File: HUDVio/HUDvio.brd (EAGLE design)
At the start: 85 x 54 mm, 16 parts, among them U1 ST_STM32F446RET7, U3 TVP5150AM1PBSR, X1 ABRACON_ABM8-27.000MHZ

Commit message: Lots of shit. Added splitter
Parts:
- added C10: 30PF_0805, Skyhawkson-Capacitors:KEMET_0805
- added C11, C12, C13: 1UF_0805, Skyhawkson-Capacitors:KEMET_0805
- added C14, C15, C16, C17, C18, C19, C20, C4, C7, C8, C9: 100NF_0805, Skyhawkson-Capacitors:KEMET_0805
- added C5, C6: 10UF_0805, Skyhawkson-Capacitors:KEMET_0805
- added R10, R11, R12, R16, R18, R9: 1K_0603, Skyhawkson-Resistors:0603
- added R13: 0R_0603, Skyhawkson-Resistors:0603
- added R14, R15: 37R4_0603, Skyhawkson-Resistors:0603
- added R17, R7, R8: 75R_0603, Skyhawkson-Resistors:0603
- added U4: NEXPERIA_NVT2006, Skyhawkson-ICs:NEXPERIA_SOT403-1_(TSSOP16)
- added U5: MAXIM_MAX4389, Skyhawkson-RF:MAXIM_21-0058_(SOT23-6)
- added X2: ABRACON_ABM8-14.31818MHZ, Skyhawkson-Miscellaneous:ABRACON_ABM8
- C1: value 1UF_0805 -> 30PF_0805
- moved C1 67.7 mm to (-76.0, -79.0)
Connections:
- removed net AGND: U2.20, U3.3, U3.31, U3.7
- removed net AVDD: U2.21, U3.32, U3.4
- removed net DGND: U3.19
- removed net DVDD: U3.20
- removed net IO_DVDD: U3.10
- removed net PGND: U2.23
- removed net PVDD: U2.24
- removed net VIDEO-OUT: U$3.3
- new net $NET11: C7.P$2, R13.1, R7.1
- new net +1V8: C16.P$2, C17.P$2, C18.P$2, C19.P$2, U3.20, U3.32, U3.4
- new net +3V3: C14.P$2, R11.1, U3.10, U4.2
- new net 5150-IN: C20.P$2, U3.1
- new net ACTIVE-VID: U3.26
- new net CS-LV: U4.3
- new net FID/GLCO: U3.23
- new net LOS-LV: U4.7
- new net LOSS-OF-SYNC: R9.1, U2.12, U4.10
- new net MAX7456-OUT: R8.2
- new net MISO-LV: U4.6
- new net MOSI-LV: U4.4
- new net N$10: C5.P$2, C6.P$2, R8.1
- new net N$11: C20.P$1, R14.2, R15.2
- new net N$12: C15.P$2, U3.2
- new net N$13: R16.1, U4.16
- new net N$14: U5.3
- new net N$15: R18.1, U5.4
- new net N$6: R10.2, U3.8
- new net N$7: R12.2, U3.28
- new net N$8: C11.P$1, C13.P$1, U3.30
- new net N$9: C11.P$2, C12.P$2, U3.29
- new net SAG: C6.P$1, U2.25
- new net SCLK-LV: U4.5
- new net SPLITTER-OUT: R14.1, R17.1, U5.1
- new net SYSCLK: U3.9
- new net VBLANK: U3.27
- new net VIDIN: C7.P$1, U2.22
- new net VIDOUT: C5.P$1, U2.26
- new net VTX-OUT: R17.2, U$3.3
- new net XTAL1: C1.P$1, U3.5, X2.1
- new net XTAL2: C10.P$1, U3.6, X2.3
- new net YOUT0: U3.18
- new net YOUT1: U3.17
- new net YOUT2: U3.16
- new net YOUT3: U3.15
- new net YOUT4: U3.14
- new net YOUT5: U3.13
- new net YOUT6: U3.12
- new net YOUT7: R11.2, U3.11
- net +5V: now also C4.P$2, C8.P$2, C9.P$2, R10.1, R12.1, R16.2, R9.2, U2.21, U2.24, U4.15, U5.6; no longer C1.P$2
- net GND: now also C1.P$2, C10.P$2, C12.P$1, C13.P$2, C14.P$1, C15.P$1, C16.P$1, C17.P$1, C18.P$1, C19.P$1, C4.P$1, C8.P$1, C9.P$1, R15.1, R18.2, R7.2, U2.20, U2.23, U3.19, U3.3, U3.31, U3.7, U4.1, U5.2, X2.2, X2.4; no longer C1.P$1
- net MAX7456-CS: now also U4.14
- net MISO: now also U4.11
- net MOSI: now also U4.13
- net SCLK: now also U4.12
- net VIDEO-IN: now also R13.2

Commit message: Ran DCMI pins
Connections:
- new net DCMI_HSYNC: U1.20, U3.25
- new net DCMI_VSYNC: U1.59, U3.24
- net SYSCLK: now also U1.22
- net YOUT0: now also U1.37
- net YOUT1: now also U1.38
- net YOUT2: now also U1.39
- net YOUT3: now also U1.40
- net YOUT4: now also U1.52
- net YOUT5: now also U1.58
- net YOUT6: now also U1.61
- net YOUT7: now also U1.62
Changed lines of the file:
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@@
 <contactref element="R5" pad="2"/>
 </signal>
-<signal name="VIDIN">
+<signal name="VIDIN" class="1">
 <contactref element="U2" pad="22"/>
 <contactref element="C7" pad="P$1"/>
 <wire x1="-61.1265" y1="-13.675" x2="-71.925" y2="-61" width="0" layer="19" extent="1-1"/>
 </signal>
-<signal name="VIDOUT">
+<signal name="VIDOUT" class="1">
 <contactref element="U2" pad="26"/>
 <contactref element="C5" pad="P$1"/>
 <wire x1="-61.1265" y1="-11.075" x2="-71.925" y2="-55" width="0" layer="19" extent="1-1"/>
 </signal>
-<signal name="MAX7456-OUT">
+<signal name="MAX7456-OUT" class="1">
 <contactref element="R8" pad="2"/>
 </signal>
@@
 <signal name="SYSCLK">
 <contactref element="U3" pad="9"/>
+<contactref element="U1" pad="22"/>
+<wire x1="-26.65" y1="3.14" x2="-47.75" y2="3.8046" width="0" layer="19" extent="1-1"/>
 </signal>
 <signal name="XTAL1">
@@
 <contactref element="R11" pad="2"/>
 <contactref element="U3" pad="11"/>
+<contactref element="U1" pad="62"/>
 <wire x1="-46.75" y1="3.8046" x2="-75.15" y2="-85" width="0" layer="19" extent="1-1"/>
+<wire x1="-28.15" y1="14.64" x2="-46.75" y2="3.8046" width="0" layer="19" extent="1-1"/>
 </signal>
 <signal name="YOUT0">
 <contactref element="U3" pad="18"/>
+<contactref element="U1" pad="37"/>
+<wire x1="-19.65" y1="7.14" x2="-42.8046" y2="5.75" width="0" layer="19" extent="1-1"/>
 </signal>
 <signal name="YOUT1">
 <contactref element="U3" pad="17"/>
+<contactref element="U1" pad="38"/>
+<wire x1="-19.65" y1="7.64" x2="-42.8046" y2="5.25" width="0" layer="19" extent="1-1"/>
 </signal>
 <signal name="YOUT2">
 <contactref element="U3" pad="16"/>
+<contactref element="U1" pad="39"/>
+<wire x1="-19.65" y1="8.14" x2="-44.25" y2="3.8046" width="0" layer="19" extent="1-1"/>
 </signal>
 <signal name="YOUT3">
 <contactref element="U3" pad="15"/>
+<contactref element="U1" pad="40"/>
+<wire x1="-19.65" y1="8.64" x2="-44.75" y2="3.8046" width="0" layer="19" extent="1-1"/>
 </signal>
 <signal name="YOUT4">
 <contactref element="U3" pad="14"/>
+<contactref element="U1" pad="52"/>
+<wire x1="-23.15" y1="14.64" x2="-45.25" y2="3.8046" width="0" layer="19" extent="1-1"/>
 </signal>
 <signal name="YOUT5">
 <contactref element="U3" pad="13"/>
+<contactref element="U1" pad="58"/>
+<wire x1="-26.15" y1="14.64" x2="-45.75" y2="3.8046" width="0" layer="19" extent="1-1"/>
 </signal>
 <signal name="YOUT6">
 <contactref element="U3" pad="12"/>
+<contactref element="U1" pad="61"/>
+<wire x1="-27.65" y1="14.64" x2="-46.25" y2="3.8046" width="0" layer="19" extent="1-1"/>
 </signal>
 <signal name="FID/GLCO">
@@
 <wire x1="-46.25" y1="10.1954" x2="-75.075" y2="-91" width="0" layer="19" extent="1-1"/>
 </signal>
-<signal name="5150-IN">
+<signal name="5150-IN" class="1">
 <contactref element="U3" pad="1"/>
 <contactref element="C20" pad="P$2"/>
@@
 <contactref element="U5" pad="3"/>
 </signal>
-<signal name="SPLITTER-OUT">
+<signal name="SPLITTER-OUT" class="1">
 <contactref element="U5" pad="1"/>
 <contactref element="R17" pad="1"/>
@@
 <wire x1="-95.7533" y1="-127.95" x2="-103.85" y2="-136" width="0" layer="19" extent="1-1"/>
 </signal>
-<signal name="VTX-OUT">
+<signal name="VTX-OUT" class="1">
 <contactref element="R17" pad="2"/>
 <contactref element="U$3" pad="3"/>
 <wire x1="-57" y1="-8" x2="-102.15" y2="-133" width="0" layer="19" extent="1-1"/>
 </signal>
+<signal name="DCMI_HSYNC">
+<contactref element="U3" pad="25"/>
+<contactref element="U1" pad="20"/>
+<wire x1="-27.65" y1="3.14" x2="-44.25" y2="10.1954" width="0" layer="19" extent="1-1"/>
+</signal>
+<signal name="DCMI_VSYNC">
+<contactref element="U3" pad="24"/>
+<contactref element="U1" pad="59"/>
+<wire x1="-26.65" y1="14.64" x2="-42.8046" y2="8.75" width="0" layer="19" extent="1-1"/>
+</signal>
 </signals>

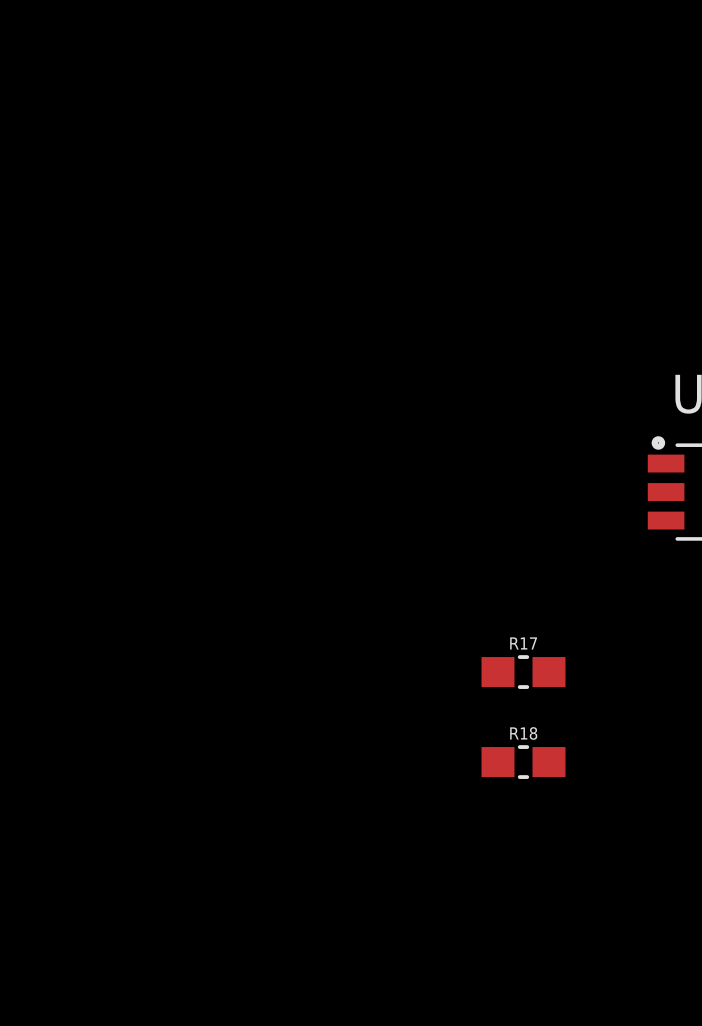
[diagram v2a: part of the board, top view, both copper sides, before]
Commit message: Added uSD card
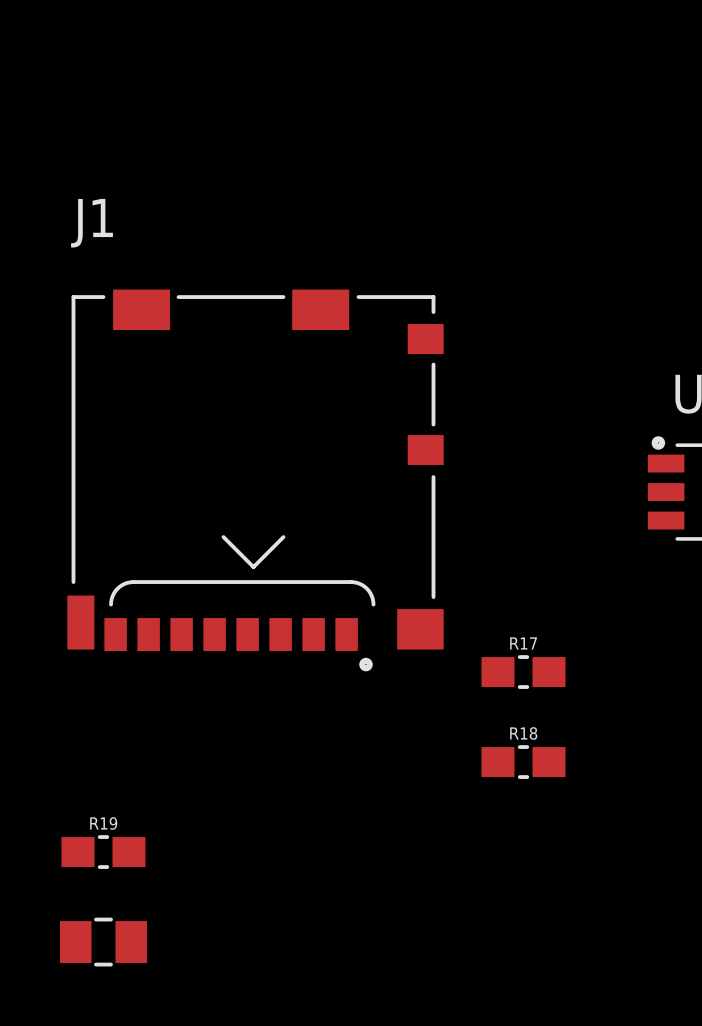
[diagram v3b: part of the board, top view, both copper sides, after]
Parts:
- added C21: 1UF_0805, Skyhawkson-Capacitors:KEMET_0805
- added J1: (no value), Skyhawkson-Connectors:MOLEX_1040310811
- added R19: 1K_0603, Skyhawkson-Resistors:0603
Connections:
- net CS-LV renamed 5150-CS
- new net CARD-DETECT: C21.P$1, J1.CD2, R19.2
- new net SD-CS: J1.P$2
- net +3V3: now also J1.CD1, J1.P$4
- net GND: now also C21.P$2, J1.G1, J1.G2, J1.G3, J1.G4, J1.P$6, R19.1
- net MISO-LV: now also J1.P$7
- net MOSI-LV: now also J1.P$3
- net SCLK-LV: now also J1.P$5
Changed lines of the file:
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@@
 <attribute name="VALUE" x="-103" y="-136.75" size="0.4064" layer="27" align="top-center"/>
+</element>
+<element name="J1" library="Skyhawkson-Connectors" library_urn="urn:adsk.eagle:library:23896875" package="MOLEX_1040310811" package3d_urn="urn:adsk.eagle:package:24291342/3" value="" x="-112" y="-132" smashed="yes">
+<attribute name="DKPN" value="WM6357CT-ND" x="-112" y="-132" size="1.778" layer="27" display="off"/>
+<attribute name="NAME" x="-118" y="-118.5" size="1.27" layer="25"/>
+<attribute name="VALUE" x="-118" y="-120" size="1.27" layer="27"/>
+</element>
+<element name="R19" library="Skyhawkson-Resistors" library_urn="urn:adsk.eagle:library:23770414" package="0603" package3d_urn="urn:adsk.eagle:package:26071182/3" value="1K_0603" x="-117" y="-139" smashed="yes">
+<attribute name="DKPN" value="311-1.00KHRCT-ND" x="-117" y="-139" size="1.778" layer="27" display="off"/>
+<attribute name="NAME" x="-117" y="-138.25" size="0.4064" layer="25" align="bottom-center"/>
+<attribute name="PACKAGE" value="0603" x="-117" y="-139" size="1.778" layer="27" display="off"/>
+<attribute name="POWER" value=".1W" x="-117" y="-139" size="1.778" layer="27" display="off"/>
+<attribute name="TOL" value="1%" x="-117" y="-139" size="1.778" layer="27" display="off"/>
+<attribute name="VAL" value="1K" x="-117" y="-139" size="1.778" layer="27" display="off"/>
+<attribute name="VALUE" x="-117" y="-139.75" size="0.4064" layer="27" align="top-center"/>
+</element>
+<element name="C21" library="Skyhawkson-Capacitors" library_urn="urn:adsk.eagle:library:23770361" package="KEMET_0805" package3d_urn="urn:adsk.eagle:package:23770363/2" value="1UF_0805" x="-117" y="-142" smashed="yes">
+<attribute name="DKPN" value="399-7409-1-ND" x="-117" y="-142" size="1.778" layer="27" display="off"/>
+<attribute name="PACKAGE" value="0805" x="-117" y="-142" size="1.778" layer="27" display="off"/>
+<attribute name="RATING" value="50V" x="-117" y="-142" size="1.778" layer="27" display="off"/>
+<attribute name="TEMP" value="X7R" x="-117" y="-142" size="1.778" layer="27" display="off"/>
+<attribute name="TOL" value="10%" x="-117" y="-142" size="1.778" layer="27" display="off"/>
+<attribute name="VAL" value="1uF" x="-117" y="-142" size="1.778" layer="27" display="off"/>
 </element>
 </elements>
@@
 <contactref element="U5" pad="2"/>
 <contactref element="R18" pad="2"/>
-<wire x1="-98.2467" y1="-127" x2="-102.15" y2="-136" width="0" layer="19" extent="1-1"/>
+<contactref element="J1" pad="G1"/>
+<contactref element="J1" pad="G4"/>
+<contactref element="J1" pad="G2"/>
+<contactref element="J1" pad="G3"/>
+<contactref element="R19" pad="1"/>
+<contactref element="C21" pad="P$2"/>
+<contactref element="J1" pad="P$6"/>
+<wire x1="-114.395" y1="-131.75" x2="-117.755" y2="-131.35" width="0" layer="19" extent="1-1"/>
+<wire x1="-117.85" y1="-139" x2="-117.755" y2="-131.35" width="0" layer="19" extent="1-1"/>
+<wire x1="-116.075" y1="-142" x2="-117.85" y2="-139" width="0" layer="19" extent="1-1"/>
+<wire x1="-106.435" y1="-131.575" x2="-114.395" y2="-131.75" width="0" layer="19" extent="1-1"/>
+<wire x1="-102.15" y1="-136" x2="-106.435" y2="-131.575" width="0" layer="19" extent="1-1"/>
+<wire x1="-98.2467" y1="-127" x2="-106.435" y2="-131.575" width="0" layer="19" extent="1-1"/>
+<wire x1="-115.73" y1="-120.925" x2="-117.755" y2="-131.35" width="0" layer="19" extent="1-1"/>
+<wire x1="-109.76" y1="-120.925" x2="-115.73" y2="-120.925" width="0" layer="19" extent="1-1"/>
 <wire x1="-85.8717" y1="-120.725" x2="-98.2467" y2="-127" width="0" layer="19" extent="1-1"/>
 <wire x1="-76.925" y1="-115" x2="-85.8717" y2="-120.725" width="0" layer="19" extent="1-1"/>
@@
 <contactref element="C14" pad="P$2"/>
 <contactref element="U4" pad="2"/>
+<contactref element="J1" pad="CD1"/>
+<contactref element="J1" pad="P$4"/>
+<wire x1="-106.26" y1="-121.9" x2="-112.195" y2="-131.75" width="0" layer="19" extent="1-1"/>
+<wire x1="-85.8717" y1="-121.375" x2="-106.26" y2="-121.9" width="0" layer="19" extent="1-1"/>
 <wire x1="-75.075" y1="-100" x2="-85.8717" y2="-121.375" width="0" layer="19" extent="1-1"/>
 <wire x1="-76.85" y1="-85" x2="-75.075" y2="-100" width="0" layer="19" extent="1-1"/>
@@
 <wire x1="-80.1283" y1="-120.725" x2="-90.85" y2="-130" width="0" layer="19" extent="1-1"/>
 </signal>
-<signal name="CS-LV">
+<signal name="5150-CS">
 <contactref element="U4" pad="3"/>
 </signal>
 <signal name="MOSI-LV">
 <contactref element="U4" pad="4"/>
+<contactref element="J1" pad="P$3"/>
+<wire x1="-85.8717" y1="-122.675" x2="-111.095" y2="-131.75" width="0" layer="19" extent="1-1"/>
 </signal>
 <signal name="SCLK-LV">
 <contactref element="U4" pad="5"/>
+<contactref element="J1" pad="P$5"/>
+<wire x1="-85.8717" y1="-123.325" x2="-113.295" y2="-131.75" width="0" layer="19" extent="1-1"/>
 </signal>
 <signal name="MISO-LV">
 <contactref element="U4" pad="6"/>
+<contactref element="J1" pad="P$7"/>
+<wire x1="-85.8717" y1="-123.975" x2="-115.495" y2="-131.75" width="0" layer="19" extent="1-1"/>
 </signal>
 <signal name="LOS-LV">
@@
 <wire x1="-26.65" y1="14.64" x2="-42.8046" y2="8.75" width="0" layer="19" extent="1-1"/>
 </signal>
+<signal name="CARD-DETECT">
+<contactref element="J1" pad="CD2"/>
+<contactref element="R19" pad="2"/>
+<contactref element="C21" pad="P$1"/>
+<wire x1="-117.925" y1="-142" x2="-116.15" y2="-139" width="0" layer="19" extent="1-1"/>
+<wire x1="-106.26" y1="-125.6" x2="-116.15" y2="-139" width="0" layer="19" extent="1-1"/>
+</signal>
+<signal name="SD-CS">
+<contactref element="J1" pad="P$2"/>
+</signal>
 </signals>

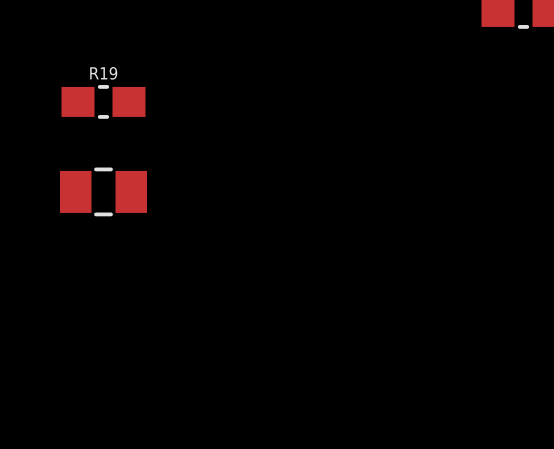
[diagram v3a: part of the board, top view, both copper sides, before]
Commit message: Assigned more pins
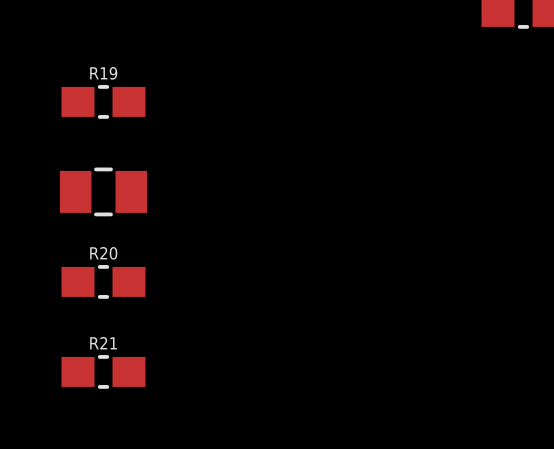
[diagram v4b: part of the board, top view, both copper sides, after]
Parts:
- added R20, R21: 2K2_0603, Skyhawkson-Resistors:0603
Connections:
- net +3V3: now also R20.2, R21.2
- net ACTIVE-VID: now also U1.53
- net FID/GLCO: now also U1.51
- net SCL: now also R20.1
- net SDA: now also R21.1
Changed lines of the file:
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@@
 <attribute name="VAL" value="1uF" x="-117" y="-142" size="1.778" layer="27" display="off"/>
+</element>
+<element name="R20" library="Skyhawkson-Resistors" library_urn="urn:adsk.eagle:library:23770414" package="0603" package3d_urn="urn:adsk.eagle:package:26071182/3" value="2K2_0603" x="-117" y="-145" smashed="yes">
+<attribute name="DKPN" value="311-2.2KGRCT-ND" x="-117" y="-145" size="1.778" layer="27" display="off"/>
+<attribute name="NAME" x="-117" y="-144.25" size="0.4064" layer="25" align="bottom-center"/>
+<attribute name="PACKAGE" value="0603" x="-117" y="-145" size="1.778" layer="27" display="off"/>
+<attribute name="POWER" value=".1W" x="-117" y="-145" size="1.778" layer="27" display="off"/>
+<attribute name="TOL" value="5%" x="-117" y="-145" size="1.778" layer="27" display="off"/>
+<attribute name="VAL" value="2K2" x="-117" y="-145" size="1.778" layer="27" display="off"/>
+<attribute name="VALUE" x="-117" y="-145.75" size="0.4064" layer="27" align="top-center"/>
+</element>
+<element name="R21" library="Skyhawkson-Resistors" library_urn="urn:adsk.eagle:library:23770414" package="0603" package3d_urn="urn:adsk.eagle:package:26071182/3" value="2K2_0603" x="-117" y="-148" smashed="yes">
+<attribute name="DKPN" value="311-2.2KGRCT-ND" x="-117" y="-148" size="1.778" layer="27" display="off"/>
+<attribute name="NAME" x="-117" y="-147.25" size="0.4064" layer="25" align="bottom-center"/>
+<attribute name="PACKAGE" value="0603" x="-117" y="-148" size="1.778" layer="27" display="off"/>
+<attribute name="POWER" value=".1W" x="-117" y="-148" size="1.778" layer="27" display="off"/>
+<attribute name="TOL" value="5%" x="-117" y="-148" size="1.778" layer="27" display="off"/>
+<attribute name="VAL" value="2K2" x="-117" y="-148" size="1.778" layer="27" display="off"/>
+<attribute name="VALUE" x="-117" y="-148.75" size="0.4064" layer="27" align="top-center"/>
 </element>
 </elements>
@@
 <signal name="SDA">
 <contactref element="U3" pad="22"/>
+<contactref element="R21" pad="1"/>
+<wire x1="-117.85" y1="-148" x2="-42.8046" y2="7.75" width="0" layer="19" extent="1-1"/>
 </signal>
 <signal name="SCL">
 <contactref element="U3" pad="21"/>
+<contactref element="R20" pad="1"/>
+<wire x1="-117.85" y1="-145" x2="-42.8046" y2="7.25" width="0" layer="19" extent="1-1"/>
 </signal>
 <signal name="VSYNC">
@@
 <signal name="ACTIVE-VID">
 <contactref element="U3" pad="26"/>
+<contactref element="U1" pad="53"/>
+<wire x1="-23.65" y1="14.64" x2="-44.75" y2="10.1954" width="0" layer="19" extent="1-1"/>
 </signal>
 <signal name="+3V3">
@@
 <contactref element="J1" pad="CD1"/>
 <contactref element="J1" pad="P$4"/>
+<contactref element="R21" pad="2"/>
+<contactref element="R20" pad="2"/>
 <wire x1="-106.26" y1="-121.9" x2="-112.195" y2="-131.75" width="0" layer="19" extent="1-1"/>
+<wire x1="-116.15" y1="-145" x2="-112.195" y2="-131.75" width="0" layer="19" extent="1-1"/>
+<wire x1="-116.15" y1="-148" x2="-116.15" y2="-145" width="0" layer="19" extent="1-1"/>
 <wire x1="-85.8717" y1="-121.375" x2="-106.26" y2="-121.9" width="0" layer="19" extent="1-1"/>
 <wire x1="-75.075" y1="-100" x2="-85.8717" y2="-121.375" width="0" layer="19" extent="1-1"/>
@@
 <signal name="FID/GLCO">
 <contactref element="U3" pad="23"/>
+<contactref element="U1" pad="51"/>
+<wire x1="-22.65" y1="14.64" x2="-42.8046" y2="8.25" width="0" layer="19" extent="1-1"/>
 </signal>
 <signal name="N$7">
